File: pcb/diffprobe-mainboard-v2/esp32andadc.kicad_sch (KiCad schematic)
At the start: 110 parts, among them J11 USB_C_Receptacle_USB2.0, J12 8P8C_LED_Shielded_x2, SW101 SW_Push, SW102 SW_Push, SW103 500SDP1S1M2QEA, U101 ESP32-S3-WROOM-1, U102 LTC2448CUHF-PBF, U103 W5500, U104 LDL1117S33R, U105 USBLC6-2SC6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

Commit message: added simulation, updated pcb designs
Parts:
- C201: value 470pF -> 470nF
- R201: value 100k -> 470R
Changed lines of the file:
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@@
 			)
 		)
-		(property "Value" "100k"
+		(property "Value" "470R"
 			(at 110.49 215.9 90)
 			(effects
@@
 			)
 		)
-		(property "Value" "470pF"
+		(property "Value" "470nF"
 			(at 100.33 223.52 90)
 			(effects

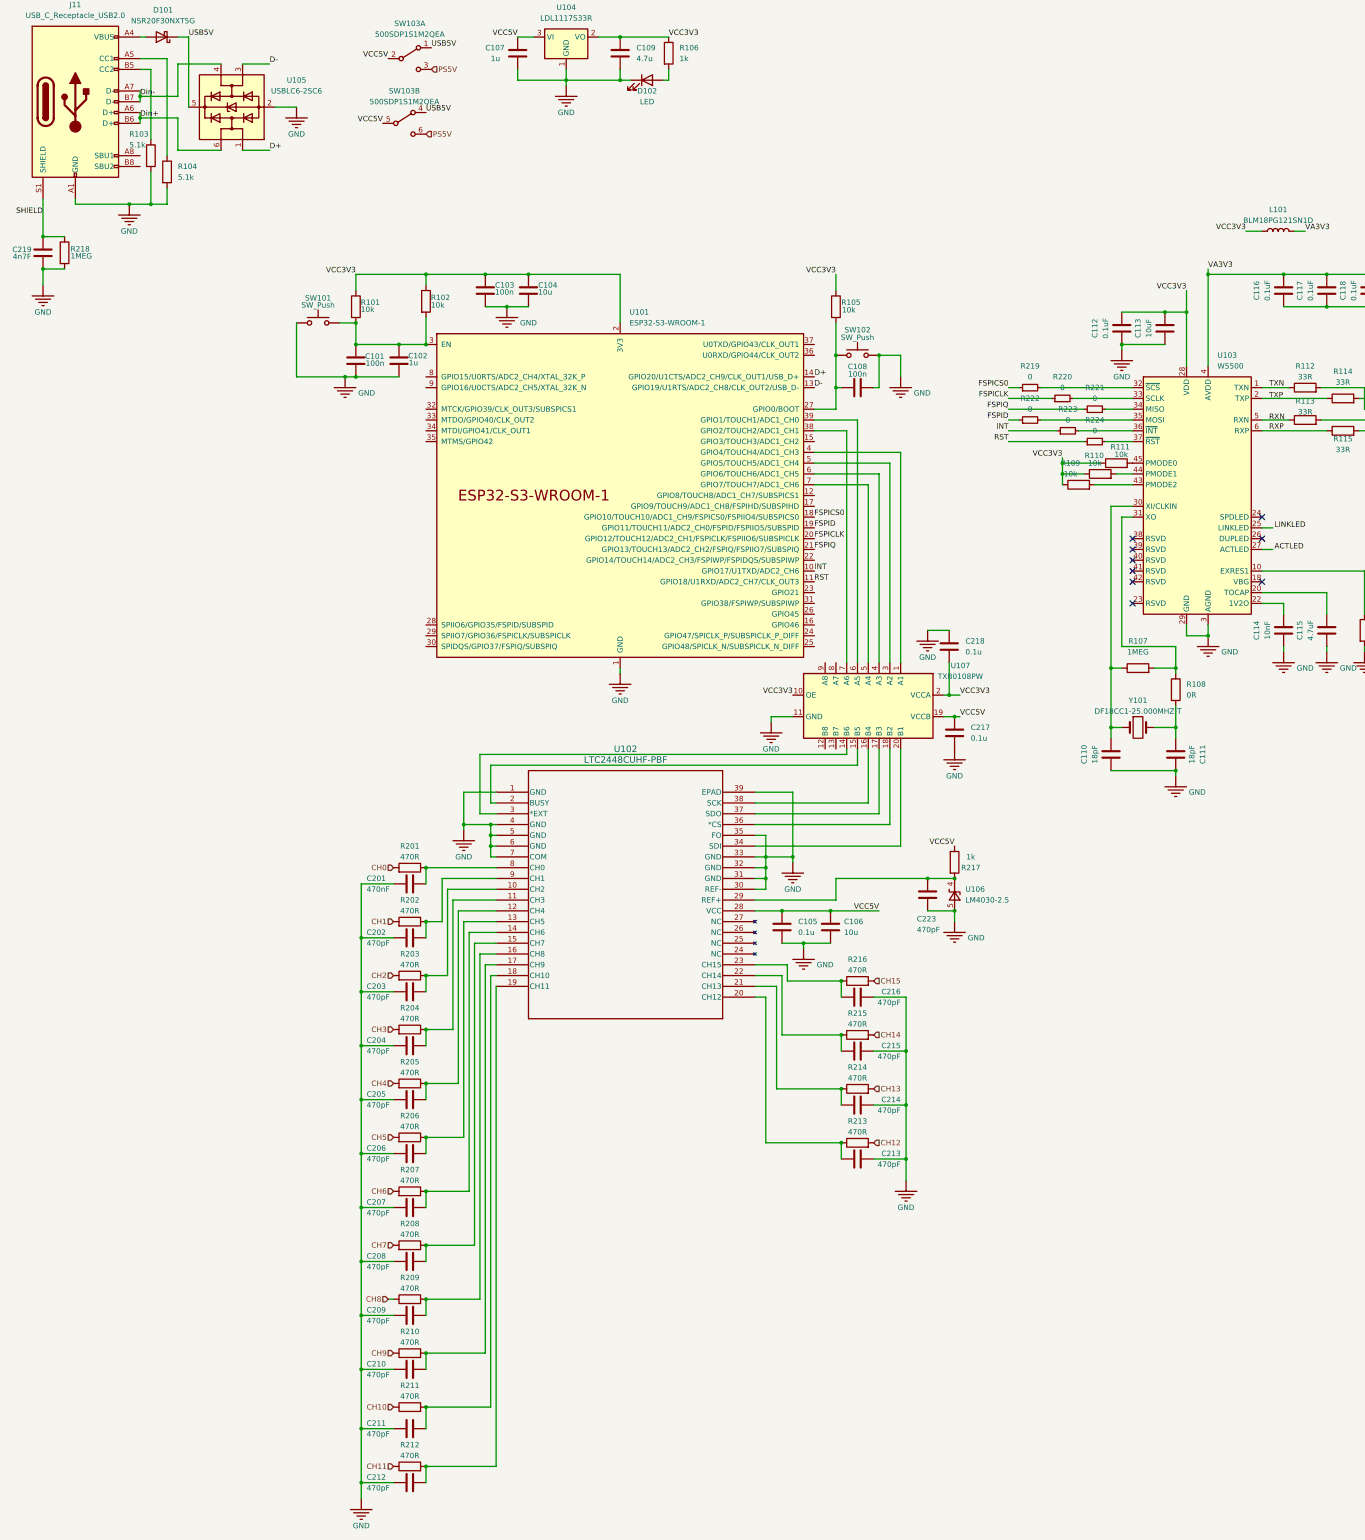
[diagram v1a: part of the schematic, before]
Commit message: KiCAD 9 update, new psu filtering and adc input signal filtering. More silkscreen writing.
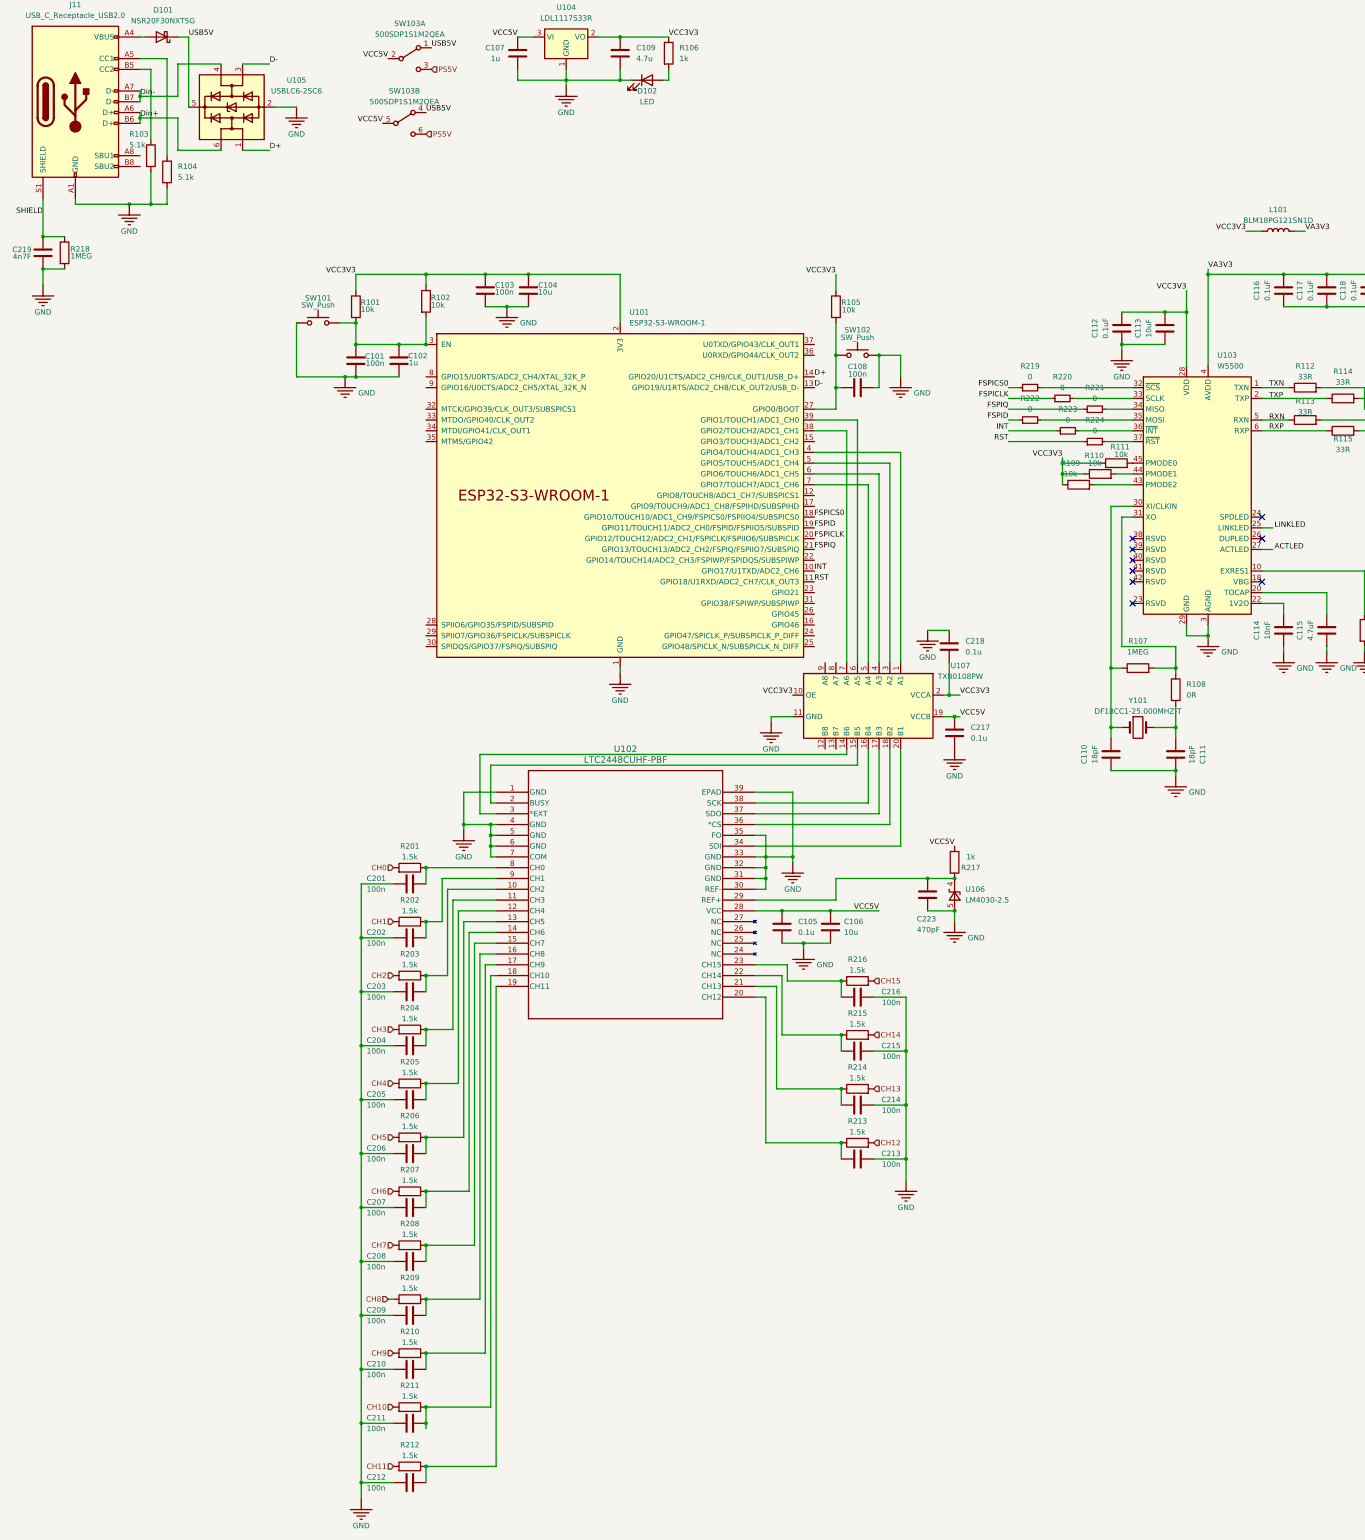
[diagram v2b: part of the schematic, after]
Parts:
- C201: value 470nF -> 100n
- C202, C203, C204, C205, C206, C207, C208, C209, C210, C211, C212, C213, C214, C215, C216: value 470pF -> 100n
- R201, R202, R203, R204, R205, R206, R207, R208, R209, R210, R211, R212, R213, R214, R215, R216: value 470R -> 1.5k
- SW101, SW102: footprint Button_Switch_SMD:SW_Push_1P1T_NO_CK_KMR2 -> Button_Switch_SMD:SW_SPST_PTS645
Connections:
- net CH10: now also R211.2; no longer R211.1
- net CH11: now also R212.2; no longer R212.1
- net CH8: now also R209.2; no longer R209.1
- net CH9: now also R210.2; no longer R210.1
- net at C210.1, U102.17 (CH9): now also R210.1; no longer R210.2
- net at C209.1, U102.16 (CH8): now also R209.1; no longer R209.2
- net at C211.1, U102.18 (CH10): now also R211.1; no longer R211.2
- net at C212.1, U102.19 (CH11): now also R212.1; no longer R212.2
